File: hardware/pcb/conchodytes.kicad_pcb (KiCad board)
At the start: 4 copper layers, 39 x 78 mm, 6 parts, among them SW1 Left click, SW2 Right Click, SW3 Middle click, U2 PMW3360

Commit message: empreinte du nRF24 rapatriée
MaeLid.pretty avait été copié depuis le fork Mouse, où il ne contient que
D_SOD-123 et LOGO : NRF24L01.kicad_mod vit dans le MaeLid du Niphargus. Le F8
de Mae a donc importé 60 composants sur 61 et laissé U8 de côté.

Vérifié dans la foulée : les 24 empreintes distinctes référencées par le schéma
sont toutes résolues dans les bibliothèques du projet.

Co-Authored-By: Claude Opus 5 <noreply@anthropic.com>
Claude-Session: https://claude.ai/code/session_01GfX5RmekmQi78Dm37qsT4Z
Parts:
- added C1: 100nF, Capacitor_SMD:C_0603_1608Metric_Pad1.08x0.95mm_HandSolder, F.Cu at (138.6, 106.7)
- added C100: 100nF, Capacitor_SMD:C_0603_1608Metric, F.Cu at (138.4, 136.1)
- added C101: 100nF, Capacitor_SMD:C_0603_1608Metric, F.Cu at (138.4, 138.7)
- added C102: 100nF, Capacitor_SMD:C_0603_1608Metric, F.Cu at (138.4, 141.2)
- added C103: 1uF, Capacitor_SMD:C_0603_1608Metric, F.Cu at (138.4, 143.7)
- added C11: 10uF, Capacitor_SMD:C_1206_3216Metric_Pad1.33x1.80mm_HandSolder, F.Cu at (143.8, 128.7)
- added C20: 10uF, Capacitor_SMD:C_1206_3216Metric_Pad1.33x1.80mm_HandSolder, F.Cu at (171.2, 107.1)
- added C21: 100nF, Capacitor_SMD:C_0603_1608Metric_Pad1.08x0.95mm_HandSolder, F.Cu at (170.4, 120.1)
- added C24: 10uF, Capacitor_SMD:C_1206_3216Metric_Pad1.33x1.80mm_HandSolder, F.Cu at (171.2, 110.4)
- added C26: 10uF, Capacitor_SMD:C_1206_3216Metric_Pad1.33x1.80mm_HandSolder, F.Cu at (171.2, 113.8)
- added C27: 1uF, Capacitor_SMD:C_0805_2012Metric_Pad1.18x1.45mm_HandSolder, F.Cu at (185.1, 116.8)
- added C29: 10uF, Capacitor_SMD:C_1206_3216Metric_Pad1.33x1.80mm_HandSolder, F.Cu at (171.2, 117.1)
- added C3: 1uF, Capacitor_SMD:C_0805_2012Metric_Pad1.18x1.45mm_HandSolder, F.Cu at (154.6, 128.5)
- added C8: 100nF, Capacitor_SMD:C_0603_1608Metric_Pad1.08x0.95mm_HandSolder, F.Cu at (138.6, 109.2)
- added D100: IR 940nm, LED_SMD:LED_0805_2012Metric, F.Cu at (143.6, 146.4)
- added D49: LED, LED_SMD:LED_0805_2012Metric_Pad1.15x1.40mm_HandSolder, F.Cu at (185.1, 113.8)
- added D52: SS14, Diode_SMD:D_SMA, F.Cu at (183.4, 121.2)
- added J1: Conn_02x03_Odd_Even, Connector_PinHeader_1.27mm:PinHeader_2x03_P1.27mm_Vertical, F.Cu at (148.9, 128.7)
- added J10: Battery, Connector_PinHeader_2.54mm:PinHeader_1x02_P2.54mm_Vertical, F.Cu at (165.8, 122.4)
- added J48: USB_C_Receptacle_USB2.0_16P, Connector_USB:USB_C_Receptacle_HRO_TYPE-C-31-M-12, F.Cu at (96.3, 74.2)
- added Q2: AO3407, Package_TO_SOT_SMD:SOT-23, F.Cu at (170.7, 128.6)
- added Q4: FS8205, Package_TO_SOT_SMD:SOT-23-6, F.Cu at (176.8, 121.3)
- added R100: 10k, Resistor_SMD:R_0603_1608Metric, F.Cu at (142.4, 136.1)
- added R101: 100, Resistor_SMD:R_0603_1608Metric, F.Cu at (142.4, 138.7)
- added R102: 270, Resistor_SMD:R_0603_1608Metric, F.Cu at (142.4, 141.2)
- added R103: 10k, Resistor_SMD:R_0603_1608Metric, F.Cu at (142.4, 143.7)
- added R104: 10k, Resistor_SMD:R_0603_1608Metric, F.Cu at (146.4, 136.1)
- added R105: 10k, Resistor_SMD:R_0603_1608Metric, F.Cu at (146.4, 138.7)
- added R106: 10k, Resistor_SMD:R_0603_1608Metric, F.Cu at (146.4, 141.2)
- added R107: 10k, Resistor_SMD:R_0603_1608Metric, F.Cu at (146.4, 143.7)
- added R16: 100, Resistor_SMD:R_0603_1608Metric_Pad0.98x0.95mm_HandSolder, F.Cu at (138.6, 114.2)
- added R18: 100, Resistor_SMD:R_0603_1608Metric_Pad0.98x0.95mm_HandSolder, F.Cu at (138.6, 116.7)
- added R2: 10k, Resistor_SMD:R_0603_1608Metric_Pad0.98x0.95mm_HandSolder, F.Cu at (138.6, 111.7)
- added R30: 100, Resistor_SMD:R_0603_1608Metric_Pad0.98x0.95mm_HandSolder, F.Cu at (138.6, 119.2)
- added R34: 10k, Resistor_SMD:R_0603_1608Metric_Pad0.98x0.95mm_HandSolder, F.Cu at (138.6, 121.7)
- added R36: 100, Resistor_SMD:R_0603_1608Metric_Pad0.98x0.95mm_HandSolder, F.Cu at (138.6, 124.2)
- added R39: 100, Resistor_SMD:R_0603_1608Metric_Pad0.98x0.95mm_HandSolder, F.Cu at (138.6, 126.7)
- added R41: 100, Resistor_SMD:R_0603_1608Metric_Pad0.98x0.95mm_HandSolder, F.Cu at (138.6, 129.2)
- added R60: 100k, Resistor_SMD:R_0603_1608Metric_Pad0.98x0.95mm_HandSolder, F.Cu at (170.4, 122.6)
- added R62: 1k, Resistor_SMD:R_0805_2012Metric_Pad1.20x1.40mm_HandSolder, F.Cu at (165.8, 106.9)
- added R64: 1M, Resistor_SMD:R_0805_2012Metric_Pad1.20x1.40mm_HandSolder, F.Cu at (165.8, 109.8)
- added R67: 1M, Resistor_SMD:R_0805_2012Metric_Pad1.20x1.40mm_HandSolder, F.Cu at (165.8, 112.8)
- added R68: 2k4, Resistor_SMD:R_0805_2012Metric_Pad1.20x1.40mm_HandSolder, F.Cu at (165.8, 115.7)
- added R70: 100, Resistor_SMD:R_0603_1608Metric_Pad0.98x0.95mm_HandSolder, F.Cu at (170.4, 125.1)
- added R73: 1k, Resistor_SMD:R_0805_2012Metric_Pad1.20x1.40mm_HandSolder, F.Cu at (165.8, 118.7)
- added R90: 5k1, Resistor_SMD:R_0603_1608Metric_Pad0.98x0.95mm_HandSolder, F.Cu at (170.8, 144.5)
- added R92: 5k1, Resistor_SMD:R_0603_1608Metric_Pad0.98x0.95mm_HandSolder, F.Cu at (170.8, 147.0)
- added SW54: SW_SPDT, Button_Switch_SMD:SW_SPDT_PCM12, F.Cu at (179.2, 108.4)
- added U100: LDO 1V8, Package_TO_SOT_SMD:SOT-23, F.Cu at (138.9, 147.2)
- added U18: TP4056-42-ESOP8, Package_SO:SOIC-8-1EP_3.9x4.9mm_P1.27mm_EP2.41x3.3mm_ThermalVias, F.Cu at (178.5, 115.7)
- added U20: HT7833, Package_TO_SOT_SMD:SOT-89-3, F.Cu at (182.8, 126.5)
- added U23: DW01A, Package_TO_SOT_SMD:SOT-23-6, F.Cu at (176.8, 125.9)
- added U54: USBLC6-2SC6, Package_TO_SOT_SMD:SOT-23-6, F.Cu at (166.0, 145.7)
- added U6: ESP32-S3-WROOM-1, PCM_Espressif:ESP32-S3-WROOM-1U, F.Cu at (105.8, 137.9)
- LD1: value Rotary illumintion -> IR encodeur
- LQ1: value EL -> photodetecteur
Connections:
- LD1 pad 1: Net-(LD1-K) -> GND
- LD1 pad 2: Pin_2J -> Net-(LD1-A)
- LQ1 pad 1: Pin_4 -> ENC_A
- LQ1 pad 2: Pin_2J -> GND
- LQ1 pad 3: GNDREF -> ENC_B
- SW1 pad 1: Net-(SW1-COM) -> GND
- SW1 pad 2: Pin_2J -> SW_LEFT
- SW2 pad 1: GNDREF -> GND
- SW2 pad 2: unconnected-(SW2-NO-Pad2) -> SW_RIGHT
- SW2 pad 3: R_NC -> unconnected-(SW2-NC-Pad3)
- SW3 pad 1: Mid_NO -> GND
- SW3 pad 2: GNDREF -> SW_MID
- SW3 pad 3: Mid_NC -> unconnected-(SW3-NC-Pad3)
- U2 pad 10: SCLK -> SCK_L
- U2 pad 11: MOSI -> MOSI_L
- U2 pad 12: MISO -> MISO_L
- U2 pad 13: CS -> SNS_NCS
- U2 pad 3: Net-(U2-VDDPIX) -> +1V8
- U2 pad 5: +3V3 -> +3.3V
- U2 pad 9: MOTION -> SNS_MOTION

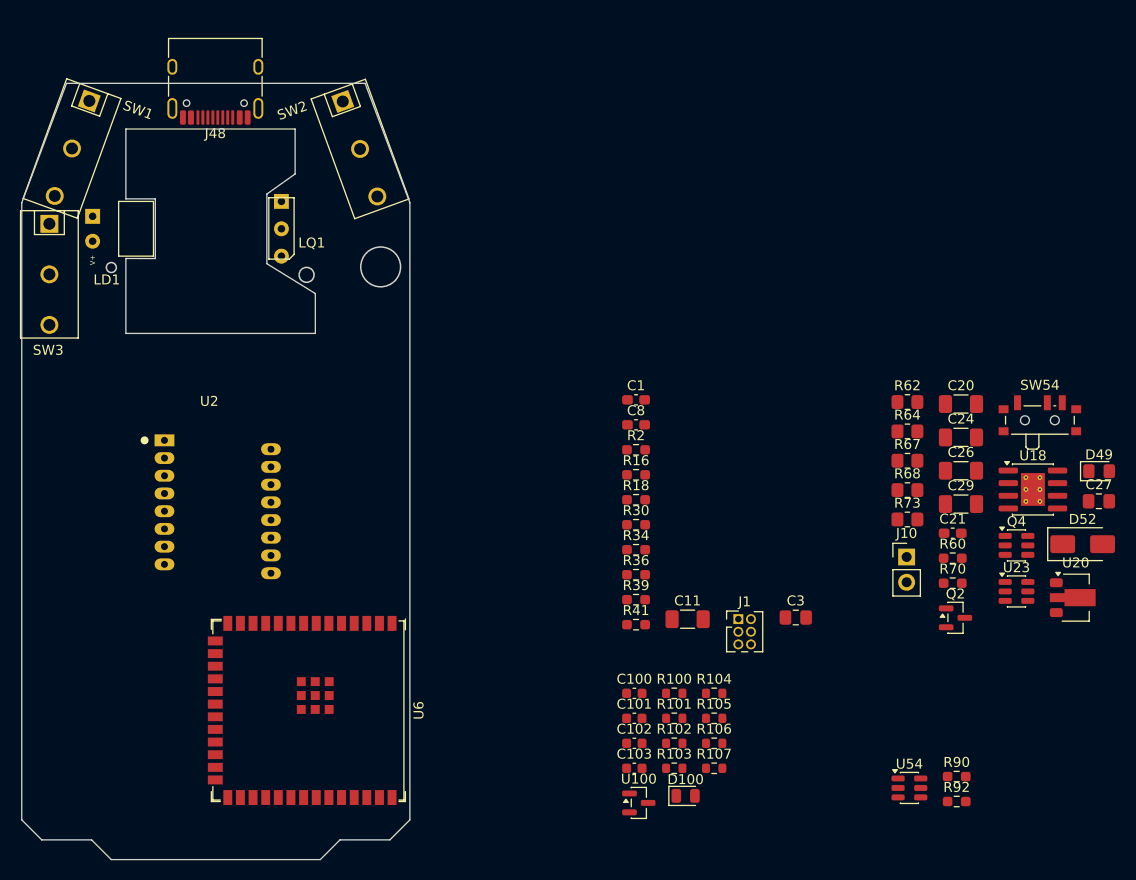
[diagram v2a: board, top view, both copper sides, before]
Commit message: contour : renflement pour le connecteur USB-C
Le J48 dépassait de 5,76 mm au-dessus du bord haut : le connecteur n'avait pas
de matière sous lui, donc pas d'USB possible. Plutôt que de le reculer — il doit
rester à l'avant, là où sortait le câble de la M100 — le contour reçoit un
renflement local : x 90,0 à 102,5, remontant de y=74,85 à y=68,5.

Le connecteur occupe x 90,98..101,62 et remonte à 69,09 : il a 0,9 mm de marge
tout autour et repose entièrement sur la carte.

Contour vérifié fermé (28 segments, zéro extrémité libre). Le PCB passe de
78 à 84,35 mm de long, la largeur reste à 39 mm — donc toujours compatible avec
les 42 mm de la zone libre du panneau Niphargus.

Piège : les coordonnées réelles étaient 81.34915 et non 81.35 (arrondi
d'affichage), et le segment était verrouillé — remplacement par parcours
balancé plutôt que par motif de texte.

Co-Authored-By: Claude Opus 5 <noreply@anthropic.com>
Claude-Session: https://claude.ai/code/session_01GfX5RmekmQi78Dm37qsT4Z
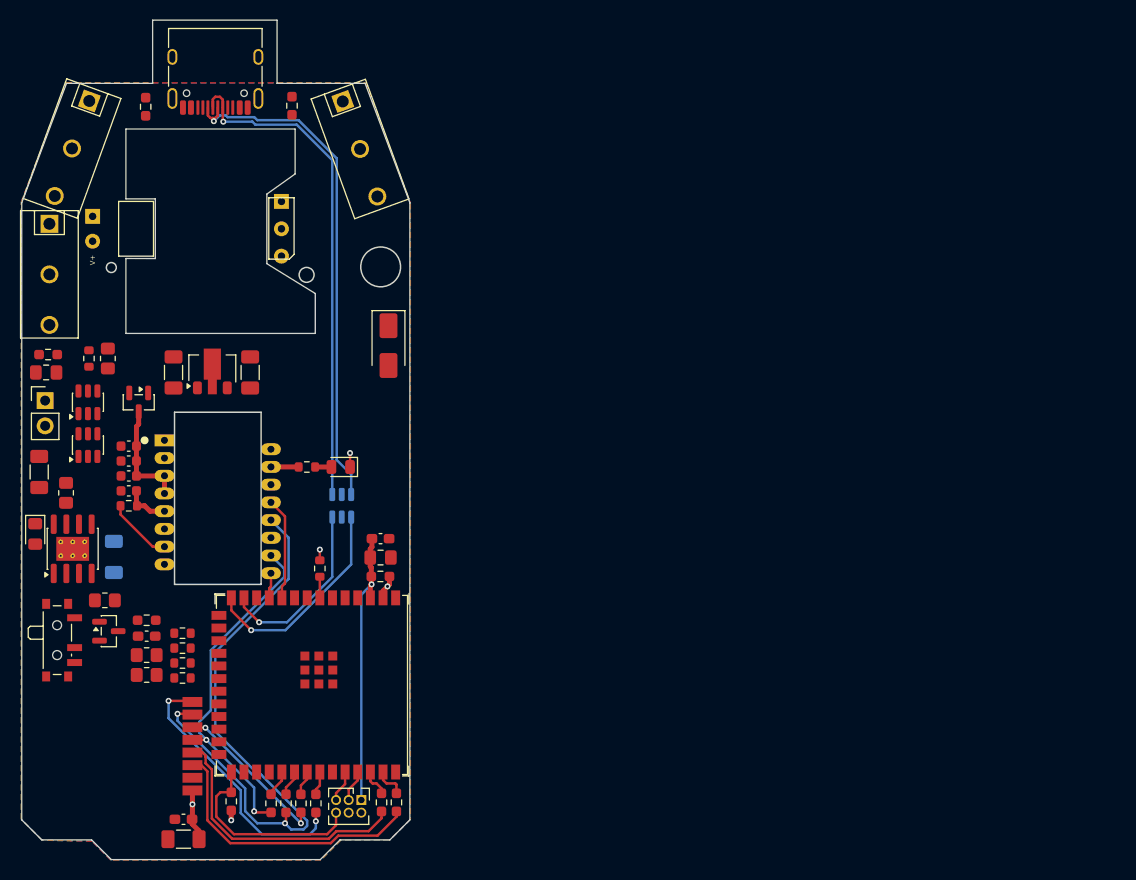
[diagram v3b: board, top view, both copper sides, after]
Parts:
- added U8: NRF24L01_Breakout, MaeLid:NRF24L01, F.Cu at (85.3, 141.5)
- C20, U54: moved to B.Cu
- moved R92 107.3 mm to (89.3, 77.2), turned to 90 degrees
- moved D49 107.1 mm to (78.2, 120.1), turned to -90 degrees
- moved C27 106.6 mm to (79.3, 103.9), turned to 180 degrees
- moved SW54 100.9 mm to (80.7, 130.8), turned to -90 degrees
- moved U18 96.7 mm to (82.0, 121.6), turned to 90 degrees
- moved U23 95.2 mm to (83.5, 106.9), turned to 90 degrees
- moved R90 94.9 mm to (104.0, 77.1), turned to -90 degrees
- moved Q4 93.8 mm to (83.5, 111.2), turned to 90 degrees
- moved R70 93.8 mm to (79.5, 102.1)
- moved C29 92.7 mm to (78.6, 113.9), turned to -90 degrees
- moved U20 89.8 mm to (96.0, 103.5), turned to 90 degrees
- moved J10 88.0 mm to (79.2, 106.7)
- moved C20 86.5 mm to (86.1, 122.4), turned to -90 degrees
- moved Q2 85.1 mm to (85.6, 129.9)
- moved R62 85.0 mm to (81.3, 116.0), turned to -90 degrees
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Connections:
- U6 pad 10: unconnected-(U6-GPIO17/U1TXD/ADC2_CH6-Pad10) -> SNS_NCS
- U6 pad 11: unconnected-(U6-GPIO18/U1RXD/ADC2_CH7/CLK_OUT3-Pad11) -> SNS_MOTION
- U6 pad 38: unconnected-(U6-GPIO2/TOUCH2/ADC1_CH1-Pad38) -> /mcu/CSN_1
- U6 pad 39: unconnected-(U6-GPIO1/TOUCH1/ADC1_CH0-Pad39) -> /mcu/CE_1
- U6 pad 4: SNS_NCS -> unconnected-(U6-GPIO4/TOUCH4/ADC1_CH3-Pad4)
- U6 pad 5: SNS_MOTION -> unconnected-(U6-GPIO5/TOUCH5/ADC1_CH4-Pad5)
- U6 pad 8: /mcu/CE_1 -> unconnected-(U6-GPIO15/U0RTS/ADC2_CH4/XTAL_32K_P-Pad8)
- U6 pad 9: /mcu/CSN_1 -> unconnected-(U6-GPIO16/U0CTS/ADC2_CH5/XTAL_32K_N-Pad9)
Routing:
- net MISO_L: track 0.00 -> 60.9 mm, vias 0 -> 2
- net Net-(J48-D+-PadA6): track 0.00 -> 52.0 mm, vias 0 -> 1
- net Net-(J48-D--PadA7): track 0.00 -> 50.4 mm, vias 0 -> 1
- net SCK_L: track 0.00 -> 35.3 mm, vias 0 -> 2
- net Net-(U8-CE): track 0.00 -> 28.3 mm
- net /mcu/EN: track 0.00 -> 28.1 mm, vias 0 -> 1
- net Net-(U8-~{CSN}): track 0.00 -> 27.5 mm
- net Net-(U8-IRQ): track 0.00 -> 27.1 mm, vias 0 -> 2
- net D+_s3: track 0.00 -> 21.6 mm, vias 0 -> 1
- net /mcu/IO0: track 0.00 -> 20.1 mm
- net D-_s3: track 0.00 -> 18.3 mm, vias 0 -> 1
- net MOSI_L: track 0.00 -> 16.0 mm, vias 0 -> 2
- net +3.3V: track 0.00 -> 15.7 mm, vias 0 -> 5
- net +1V8: track 0.00 -> 11.2 mm
- net SNS_NCS: track 0.00 -> 10.3 mm
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- added copper zone on In2.Cu, net +3.3V
- added copper zone on B.Cu, net GND
- added copper zone on F.Cu, net GND
- added copper zone on In1.Cu, net GND
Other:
- board size 39 x 78 mm -> 39 x 84.3 mm

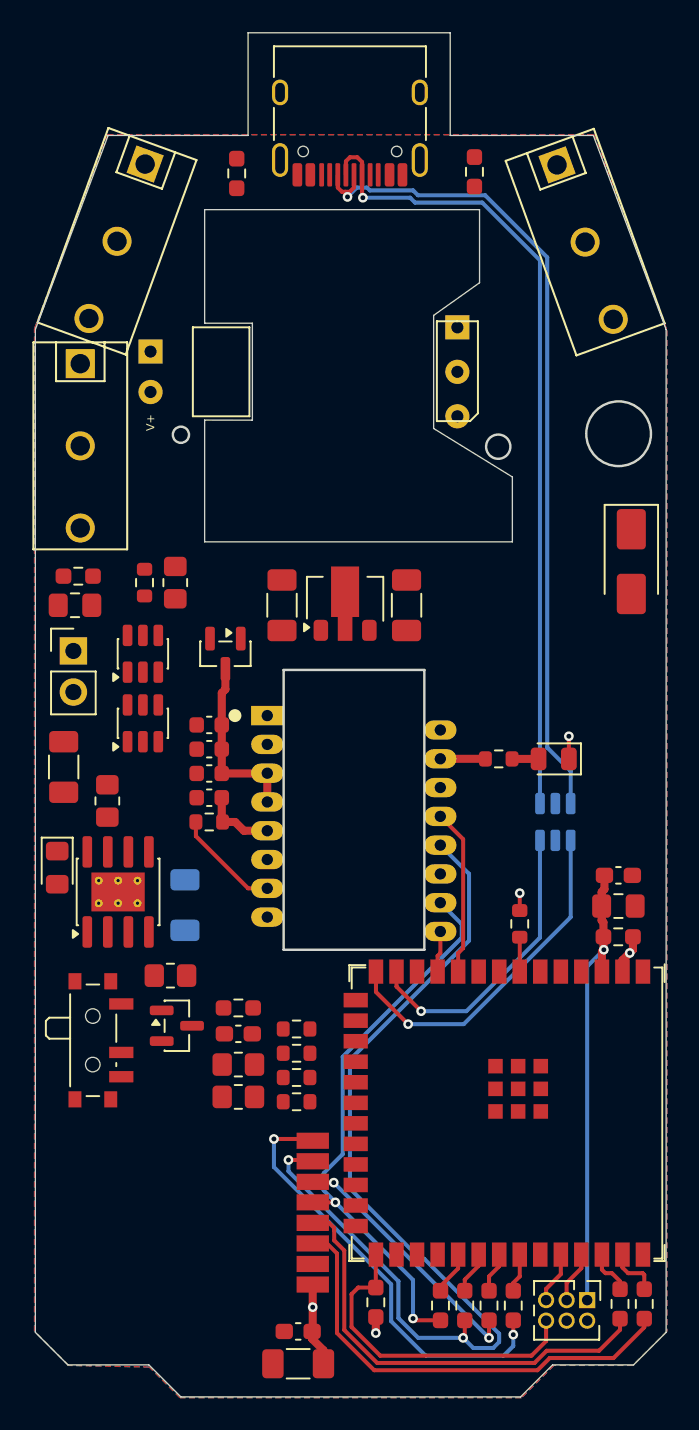
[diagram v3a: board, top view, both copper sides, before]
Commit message: logos Niphargus importés dans la bibliothèque
Les 5 empreintes de logo vivaient seulement dans le MaeLid du clavier — le
MaeLid de Conchodytes venait du fork Mouse, qui ne contient que D_SOD-123 et
LOGO. Même cause que le nRF24 manquant au premier F8.

Copiées : Niphargus_10mm_Cu et _silk (8,8 x 9,0 mm — la crevette),
niphargus_19mm_silk (17,7 x 18,1), Niphargus_text_3mm_Cu et _silk
(15,6 x 3,9 — le mot). Sur le clavier, HS1/HS2 utilisent la version cuivre au
dos et HS3 le texte en sérigraphie à l'avant.

Rien n'est posé sur la carte : Mae les placera elle-même. fp-lib-table
inchangée, MaeLid y était déjà déclarée et reste résolue.

Co-Authored-By: Claude Opus 5 <noreply@anthropic.com>
Claude-Session: https://claude.ai/code/session_01GfX5RmekmQi78Dm37qsT4Z
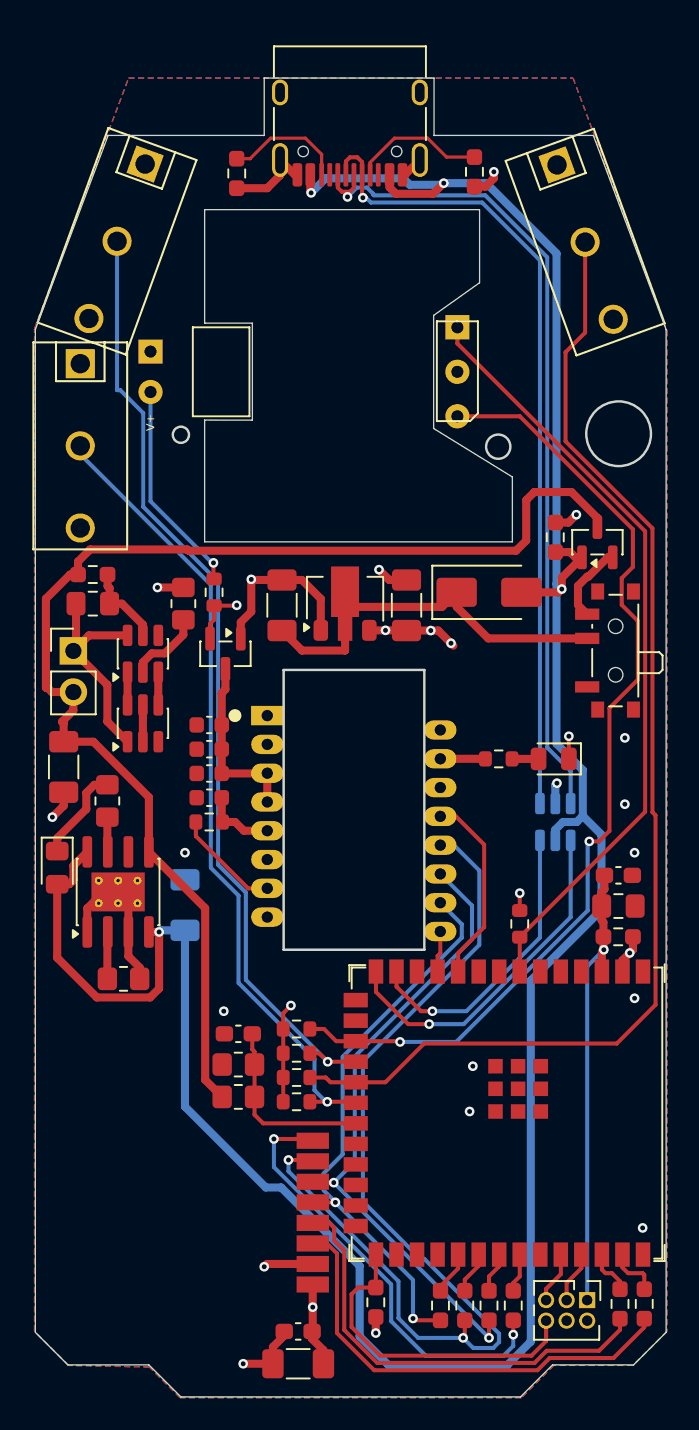
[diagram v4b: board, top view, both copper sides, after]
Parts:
- moved SW54 39.8 mm to (112.4, 106.7), turned to 90 degrees
- moved Q2 39.6 mm to (111.6, 100.0), turned to 90 degrees
- moved R60 35.1 mm to (109.0, 99.7), turned to -90 degrees
- moved D52 9.00 mm to (104.9, 103.1), turned to 0 degrees
- moved R102 4.34 mm to (87.9, 103.1)
- moved R68 2.91 mm to (82.3, 127.0)
- moved R73 1.39 mm to (86.0, 103.8)
- moved C27 1.10 mm to (80.4, 103.8)
- moved R70 0.91 mm to (80.4, 102.0)
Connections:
- SW54 pad 2: Net-(Q2-S) -> Net-(D52-K)
- SW54 pad 3: Net-(D52-K) -> Net-(Q2-S)
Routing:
- net +5V: track 0.00 -> 166.5 mm, vias 0 -> 4
- net +BATT: track 0.00 -> 77.9 mm
- net SW_RIGHT: track 0.00 -> 73.4 mm
- net ENC_B: track 0.00 -> 60.5 mm, vias 0 -> 2
- net SW_LEFT: track 0.00 -> 59.3 mm, vias 0 -> 1
- net SW_MID: track 0.00 -> 49.8 mm, vias 0 -> 1
- net ENC_A: track 2.12 -> 47.9 mm
- net GND: track 0.00 -> 44.5 mm, vias 0 -> 18
- net Net-(D52-K): track 0.00 -> 23.9 mm
- net MOSI_L: track 16.0 -> 39.4 mm
- net +3.3V: track 15.7 -> 31.1 mm, vias 5 -> 10
- net -BATT: track 0.00 -> 13.7 mm
- net Net-(LD1-A): track 0.00 -> 13.4 mm, vias 0 -> 1
- net VBAT_SENSE: track 0.00 -> 11.5 mm
- net Net-(J48-CC1): track 0.00 -> 8.32 mm
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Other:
- board size 39 x 84.3 mm -> 39 x 81.5 mm

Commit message: baseline re-référencée sur le projet complet
L'ancienne baseline (ERC 1/93, DRC 4/11) datait du jour où le dépôt ne contenait
que le contour et les 6 empreintes de la coque : elle comparait à un état qui
n'avait plus de sens et gardait le check au rouge en permanence, donc sans
valeur d'alerte.

Nouvelle référence sur le projet schématisé, importé et routé :
  ERC 14 erreurs / 14 warnings     DRC 26 erreurs / 19 warnings

Ce ne sont PAS des cotes acceptables, c'est un point de départ. Le ratchet
enregistrera automatiquement chaque baisse. Objectif zéro, comme sur le clavier.

Ce qu'il reste dedans :
- DRC : 18 copper_edge_clearance (dont 2 seulement dues au renflement USB),
  10 silk_edge_clearance, 7 starved_thermal, 7 copper_sliver ;
- ERC : 13 pin_not_connected (GPIO libres du S3, à marquer no-connect),
  11 pin_to_pin (les pins du symbole Optical_Mouse importé du KiCad 5 sont de
  type « non spécifié »), 1 power_pin_not_driven (PWR_FLAG du +5V).

check.sh complet vert.

Co-Authored-By: Claude Opus 5 <noreply@anthropic.com>
Claude-Session: https://claude.ai/code/session_01GfX5RmekmQi78Dm37qsT4Z
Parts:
- added REF**: nephargus_10mm_Cu, MaeLid:Niphargus_10mm_Cu, B.Cu at (87.5, 144.5)
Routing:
- net GND: track 44.5 -> 46.3 mm
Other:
- board text added: "Conchodytes"
- board text added: "V1"
